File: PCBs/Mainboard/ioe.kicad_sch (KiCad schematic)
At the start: 2 parts, among them IC3 TCA6408ARSVR

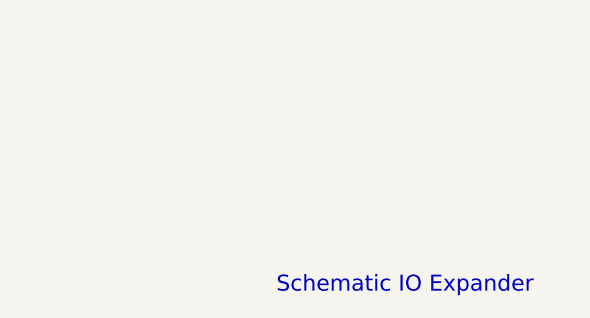
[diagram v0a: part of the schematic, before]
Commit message: Add progress report for 31.1.2025 Update relevant source files
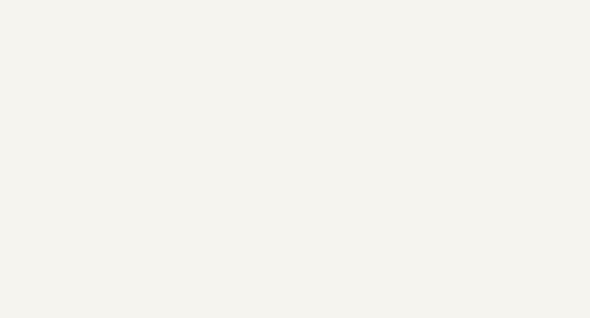
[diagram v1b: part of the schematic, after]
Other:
- note removed: "Schematic IO Expander"
- title: (none) -> IO Expander
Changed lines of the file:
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@@
 	(generator_version "8.0")
 	(paper "A4")
+	(title_block
+		(title "IO Expander")
+	)
 	(junction
 		(at 67.31 55.88)
@@
 		)
 	)
-	(text "Schematic IO Expander"
-		(exclude_from_sim no)
-		(at 202.438 189.738 0)
-		(effects
-			(font
-				(size 1.778 1.778)
-			)
-		)
-	)
 	(hierarchical_label "SCL"
 		(shape input)
 		(at 85.09 71.12 0)
-		(fields_autoplaced yes)
 		(effects
 			(font
@@
 		(shape input)
 		(at 54.61 73.66 180)
-		(fields_autoplaced yes)
 		(effects
 			(font
@@
 		(shape input)
 		(at 72.39 93.98 270)
-		(fields_autoplaced yes)
 		(effects
 			(font
@@
 		(shape input)
 		(at 85.09 78.74 0)
-		(fields_autoplaced yes)
 		(effects
 			(font
@@
 		(shape input)
 		(at 85.09 76.2 0)
-		(fields_autoplaced yes)
 		(effects
 			(font
@@
 		(shape input)
 		(at 64.77 93.98 270)
-		(fields_autoplaced yes)
 		(effects
 			(font
@@
 		(shape input)
 		(at 69.85 93.98 270)
-		(fields_autoplaced yes)
 		(effects
 			(font
@@
 		(shape input)
 		(at 54.61 78.74 180)
-		(fields_autoplaced yes)
 		(effects
 			(font
@@
 		(shape input)
 		(at 85.09 73.66 0)
-		(fields_autoplaced yes)
 		(effects
 			(font
@@
 		(shape input)
 		(at 72.39 55.88 90)
-		(fields_autoplaced yes)
 		(effects
 			(font
@@
 		(shape input)
 		(at 54.61 76.2 180)
-		(fields_autoplaced yes)
 		(effects
 			(font
